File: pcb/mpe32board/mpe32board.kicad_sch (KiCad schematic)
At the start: 42 parts, among them J1 Conn_ST_STDC14, J2 USB_C_Receptacle_USB2.0_16P, J46 Conn_02x10_Counter_Clockwise, SW1 SW_Push, SW2 SW_Push, U10 W9812G6KH-75, U2 USBLC6-2P6, U3 AMS1117-3.3, U9 STM32H743IITx

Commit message: length match sdram
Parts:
- removed C1: 4.7μF, Capacitor_SMD:C_0603_1608Metric, symbol Device:C_Small
- added C35, C36, C37, C38, C39, C40, C41: 100nF, Capacitor_SMD:C_0603_1608Metric, symbol Device:C_Small
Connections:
- net +3V3: now also C35.1, C36.1, C37.1, C38.1, C39.1, C40.1, C41.1
- net BTN1_INTERNAL: now also U9.110 (PG6); no longer U9.99 (PD11)
- net BTN2_INTERNAL: now also U9.111 (PG7); no longer U9.100 (PD12)
- net GND: now also C35.2, C36.2, C37.2, C38.2, C39.2, C40.2, C41.2
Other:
- note removed: "extra for vdd"

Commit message: silkscreen for main board + finished sensor board
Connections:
- net +3V3: now also J46.11 (Pin_11); no longer J46.1 (Pin_1)
- net GND: now also J46.1 (Pin_1); no longer J46.11 (Pin_11)
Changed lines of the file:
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@@
 	(wire
 		(pts
-			(xy 143.51 62.23) (xy 143.51 63.5)
-		)
-		(stroke
-			(width 0)
-			(type default)
-		)
-	)
-	(wire
-		(pts
 			(xy 316.23 135.89) (xy 326.39 135.89)
 		)
@@
 	(wire
 		(pts
+			(xy 166.37 92.71) (xy 166.37 93.98)
+		)
+		(stroke
+			(width 0)
+			(type default)
+		)
+	)
+	(wire
+		(pts
 			(xy 361.95 125.73) (xy 361.95 127)
 		)
@@
 	(wire
 		(pts
-			(xy 161.29 87.63) (xy 161.29 86.36)
+			(xy 161.29 86.36) (xy 161.29 93.98)
 		)
 		(stroke
@@
 	(wire
 		(pts
+			(xy 166.37 93.98) (xy 161.29 93.98)
+		)
+		(stroke
+			(width 0)
+			(type default)
+		)
+	)
+	(wire
+		(pts
 			(xy 231.14 43.18) (xy 241.3 43.18)
 		)
@@
 	(wire
 		(pts
+			(xy 139.7 58.42) (xy 139.7 57.15)
+		)
+		(stroke
+			(width 0)
+			(type default)
+		)
+	)
+	(wire
+		(pts
 			(xy 241.3 48.26) (xy 251.46 48.26)
 		)
@@
 	(wire
 		(pts
+			(xy 143.51 57.15) (xy 143.51 63.5)
+		)
+		(stroke
+			(width 0)
+			(type default)
+		)
+	)
+	(wire
+		(pts
 			(xy 241.3 43.18) (xy 251.46 43.18)
 		)
@@
 	(wire
 		(pts
+			(xy 139.7 57.15) (xy 143.51 57.15)
+		)
+		(stroke
+			(width 0)
+			(type default)
+		)
+	)
+	(wire
+		(pts
 			(xy 36.83 234.95) (xy 36.83 233.68)
 		)
@@
 	(symbol
 		(lib_id "power:+3V3")
+		(at 166.37 92.71 0)
+		(unit 1)
+		(body_style 1)
+		(exclude_from_sim no)
+		(in_bom yes)
+		(on_board yes)
+		(in_pos_files yes)
+		(dnp no)
+		(fields_autoplaced yes)
+		(property "Reference" "#PWR0184"
+			(at 166.37 96.52 0)
+			(hide yes)
+			(show_name no)
+			(do_not_autoplace no)
+			(effects
+				(font
+					(size 1.27 1.27)
+				)
+			)
+		)
+		(property "Value" "+3V3"
+			(at 166.37 87.63 0)
+			(show_name no)
+			(do_not_autoplace no)
+			(effects
+				(font
+					(size 1.27 1.27)
+				)
+			)
+		)
+		(property "Footprint" ""
+			(at 166.37 92.71 0)
+			(hide yes)
+			(show_name no)
+			(do_not_autoplace no)
+			(effects
+				(font
+					(size 1.27 1.27)
+				)
+			)
+		)
+		(property "Datasheet" ""
+			(at 166.37 92.71 0)
+			(hide yes)
+			(show_name no)
+			(do_not_autoplace no)
+			(effects
+				(font
+					(size 1.27 1.27)
+				)
+			)
+		)
+		(property "Description" "Power symbol creates a global label with name \"+3V3\""
+			(at 166.37 92.71 0)
+			(hide yes)
+			(show_name no)
+			(do_not_autoplace no)
+			(effects
+				(font
+					(size 1.27 1.27)
+				)
+			)
+		)
+		(pin "1"
+		)
+		(instances
+			(project "mpe32board"
+				(path "/90f9def3-561d-490b-a661-0a19546ece9e"
+					(reference "#PWR0184")
+					(unit 1)
+				)
+			)
+		)
+	)
+	(symbol
+		(lib_id "power:+3V3")
 		(at 250.19 60.96 0)
 		(unit 1)
@@
 	(symbol
 		(lib_id "power:GND")
+		(at 139.7 58.42 0)
+		(unit 1)
+		(body_style 1)
+		(exclude_from_sim no)
+		(in_bom yes)
+		(on_board yes)
+		(in_pos_files yes)
+		(dnp no)
+		(property "Reference" "#PWR0180"
+			(at 139.7 64.77 0)
+			(hide yes)
+			(show_name no)
+			(do_not_autoplace no)
+			(effects
+				(font
+					(size 1.27 1.27)
+				)
+			)
+		)
+		(property "Value" "GND"
+			(at 139.7 62.992 0)
+			(show_name no)
+			(do_not_autoplace no)
+			(effects
+				(font
+					(size 1.27 1.27)
+				)
+			)
+		)
+		(property "Footprint" ""
+			(at 139.7 58.42 0)
+			(hide yes)
+			(show_name no)
+			(do_not_autoplace no)
+			(effects
+				(font
+					(size 1.27 1.27)
+				)
+			)
+		)
+		(property "Datasheet" ""
+			(at 139.7 58.42 0)
+			(hide yes)
+			(show_name no)
+			(do_not_autoplace no)
+			(effects
+				(font
+					(size 1.27 1.27)
+				)
+			)
+		)
+		(property "Description" "Power symbol creates a global label with name \"GND\" , ground"
+			(at 139.7 58.42 0)
+			(hide yes)
+			(show_name no)
+			(do_not_autoplace no)
+			(effects
+				(font
+					(size 1.27 1.27)
+				)
+			)
+		)
+		(pin "1"
+		)
+		(instances
+			(project "mpe32board"
+				(path "/90f9def3-561d-490b-a661-0a19546ece9e"
+					(reference "#PWR0180")
+					(unit 1)
+				)
+			)
+		)
+	)
+	(symbol
+		(lib_id "power:GND")
 		(at 31.75 236.22 0)
 		(unit 1)
@@
 	)
 	(symbol
-		(lib_id "power:+3V3")
-		(at 143.51 62.23 0)
-		(unit 1)
-		(body_style 1)
-		(exclude_from_sim no)
-		(in_bom yes)
-		(on_board yes)
-		(in_pos_files yes)
-		(dnp no)
-		(fields_autoplaced yes)
-		(property "Reference" "#PWR0179"
-			(at 143.51 66.04 0)
-			(hide yes)
-			(show_name no)
-			(do_not_autoplace no)
-			(effects
-				(font
-					(size 1.27 1.27)
-				)
-			)
-		)
-		(property "Value" "+3V3"
-			(at 143.51 57.15 0)
-			(show_name no)
-			(do_not_autoplace no)
-			(effects
-				(font
-					(size 1.27 1.27)
-				)
-			)
-		)
-		(property "Footprint" ""
-			(at 143.51 62.23 0)
-			(hide yes)
-			(show_name no)
-			(do_not_autoplace no)
-			(effects
-				(font
-					(size 1.27 1.27)
-				)
-			)
-		)
-		(property "Datasheet" ""
-			(at 143.51 62.23 0)
-			(hide yes)
-			(show_name no)
-			(do_not_autoplace no)
-			(effects
-				(font
-					(size 1.27 1.27)
-				)
-			)
-		)
-		(property "Description" "Power symbol creates a global label with name \"+3V3\""
-			(at 143.51 62.23 0)
-			(hide yes)
-			(show_name no)
-			(do_not_autoplace no)
-			(effects
-				(font
-					(size 1.27 1.27)
-				)
-			)
-		)
-		(pin "1"
-		)
-		(instances
-			(project "mpe32board"
-				(path "/90f9def3-561d-490b-a661-0a19546ece9e"
-					(reference "#PWR0179")
-					(unit 1)
-				)
-			)
-		)
-	)
-	(symbol
 		(lib_id "Device:C_Small")
 		(at 298.45 59.69 0)
@@
 					(unit 1)
 				)
-			)
-		)
-	)
-	(symbol
-		(lib_id "power:GND")
-		(at 161.29 87.63 0)
-		(unit 1)
-		(body_style 1)
-		(exclude_from_sim no)
-		(in_bom yes)
-		(on_board yes)
-		(in_pos_files yes)
-		(dnp no)
-		(property "Reference" "#PWR0180"
-			(at 161.29 93.98 0)
-			(hide yes)
-			(show_name no)
-			(do_not_autoplace no)
-			(effects
-				(font
-					(size 1.27 1.27)
-				)
-			)
-		)
-		(property "Value" "GND"
-			(at 160.02 92.202 0)
-			(show_name no)
-			(do_not_autoplace no)
-			(effects
-				(font
-					(size 1.27 1.27)
-				)
-			)
-		)
-		(property "Footprint" ""
-			(at 161.29 87.63 0)
-			(hide yes)
-			(show_name no)
-			(do_not_autoplace no)
-			(effects
-				(font
-					(size 1.27 1.27)
-				)
-			)
-		)
-		(property "Datasheet" ""
-			(at 161.29 87.63 0)
-			(hide yes)
-			(show_name no)
-			(do_not_autoplace no)
-			(effects
-				(font
-					(size 1.27 1.27)
-				)
-			)
-		)
-		(property "Description" "Power symbol creates a global label with name \"GND\" , ground"
-			(at 161.29 87.63 0)
-			(hide yes)
-			(show_name no)
-			(do_not_autoplace no)
-			(effects
-				(font
-					(size 1.27 1.27)
-				)
-			)
-		)
-		(pin "1"
-		)
-		(instances
-			(project "mpe32board"
-				(path "/90f9def3-561d-490b-a661-0a19546ece9e"
-					(reference "#PWR0180")
-					(unit 1)
-				)

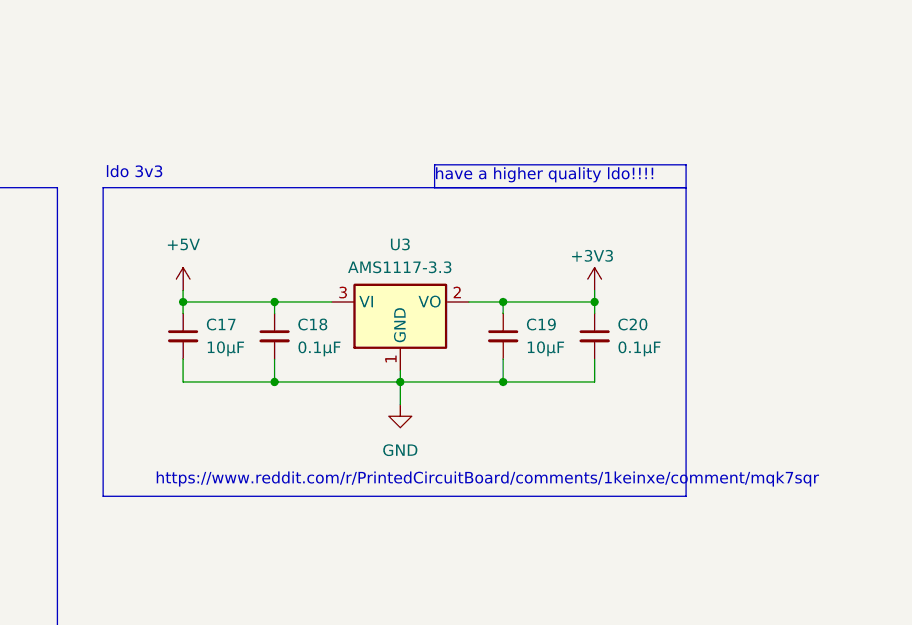
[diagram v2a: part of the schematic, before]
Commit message: add lcd level shifter, lm1117 ldo
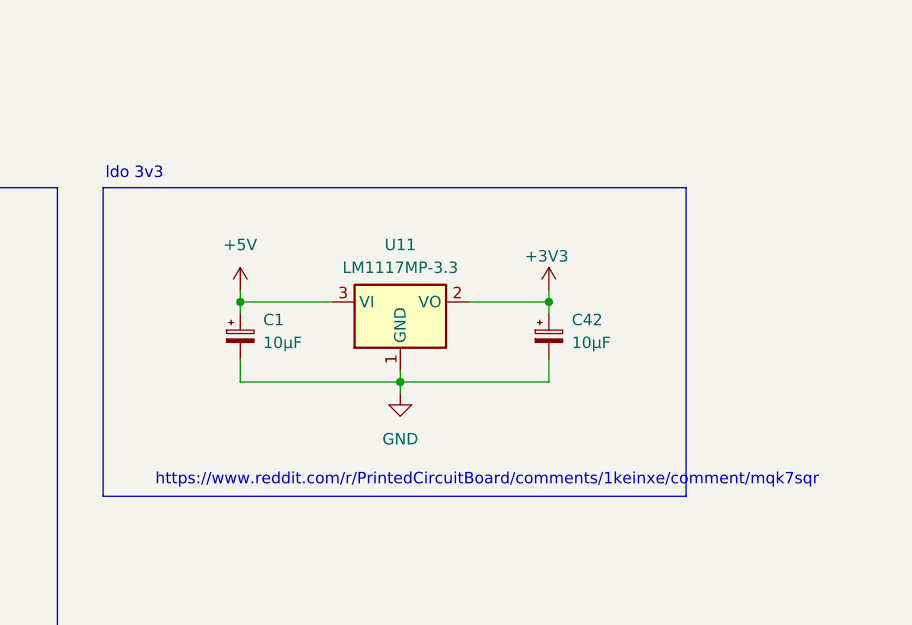
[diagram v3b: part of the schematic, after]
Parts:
- removed C17, C19: 10μF, Capacitor_SMD:C_0603_1608Metric, symbol Device:C_Small
- removed C18, C20: 0.1μF, Capacitor_SMD:C_0603_1608Metric, symbol Device:C_Small
- removed U3: AMS1117-3.3, Package_TO_SOT_SMD:SOT-223-3_TabPin2, symbol Regulator_Linear:AMS1117-3.3
- added C1, C42: 10μF, Capacitor_SMD:C_1206_3216Metric, symbol Device:C_Polarized_Small
- added U11: LM1117MP-3.3, Package_TO_SOT_SMD:SOT-223-3_TabPin2, symbol Regulator_Linear:LM1117MP-3.3
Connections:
- net +3V3: now also C42.1, U11.2 (VO)
- net +5V: now also C1.1, U11.3 (VI)
- net GND: now also C1.2, C42.2, U11.1 (GND)
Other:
- note removed: "have a higher quality ldo!!!!"

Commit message: fix power scheme and add usb diode + more
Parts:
- added C17: 100nF, Capacitor_SMD:C_0603_1608Metric, symbol Device:C_Small
- added C43: 1μF, Capacitor_SMD:C_0603_1608Metric, symbol Device:C_Small
- added D1: SS14, Diode_SMD:D_SMA, symbol Diode:SS14
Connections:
- net +3V3: now also C17.1, C43.1
- net +5V: now also D1.1 (K); no longer J2.A4 (VBUS), J2.A9 (VBUS), J2.B4 (VBUS), J2.B9 (VBUS)
- net GND: now also C17.2, C43.2
- new net: D1.2 (A), J2.A4 (VBUS), J2.A9 (VBUS), J2.B4 (VBUS), J2.B9 (VBUS)
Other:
- note added: "for vref+"
- note removed: "optional 100nF + 1x1μF"
